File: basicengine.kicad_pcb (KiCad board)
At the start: 2 copper layers, 85 x 56 mm, 114 parts, among them J1 MicroSD Card, J10 Conn_01x01, J12 Conn_02x20_Counter_Clockwise, J17 PSX CONTROLLER, J2 USB KBD Alt, J3 Conn_01x06, J4 Conn_01x03, J5 VIDEO, J6 USB KBD, J7 AUDIO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

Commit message: pcb: add OSHW logo
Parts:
- added REF***: OSHW-Logo2_7.3x6mm_SilkScreen, Symbols:OSHW-Logo2_7.3x6mm_SilkScreen, B.Cu at (105.7, 118.3)

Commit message: pcb: follow sch oscillator capacitor change from 10p to 56p
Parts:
- C3, C4: value 10p -> 56p
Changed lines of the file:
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@@
       (effects (font (size 0.8128 0.8128) (thickness 0.15)) (justify mirror))
     )
-    (fp_text value 10p (at 1.63 -1.75 360) (layer B.SilkS)
+    (fp_text value 56p (at 1.63 -1.75 360) (layer B.SilkS)
       (effects (font (size 0.8128 0.8128) (thickness 0.15)) (justify mirror))
     )
@@
       (effects (font (size 0.8128 0.8128) (thickness 0.15)) (justify mirror))
     )
-    (fp_text value 10p (at -1.64 -1.65 180) (layer B.SilkS)
+    (fp_text value 56p (at -1.64 -1.65 180) (layer B.SilkS)
       (effects (font (size 0.8128 0.8128) (thickness 0.15)) (justify mirror))
     )

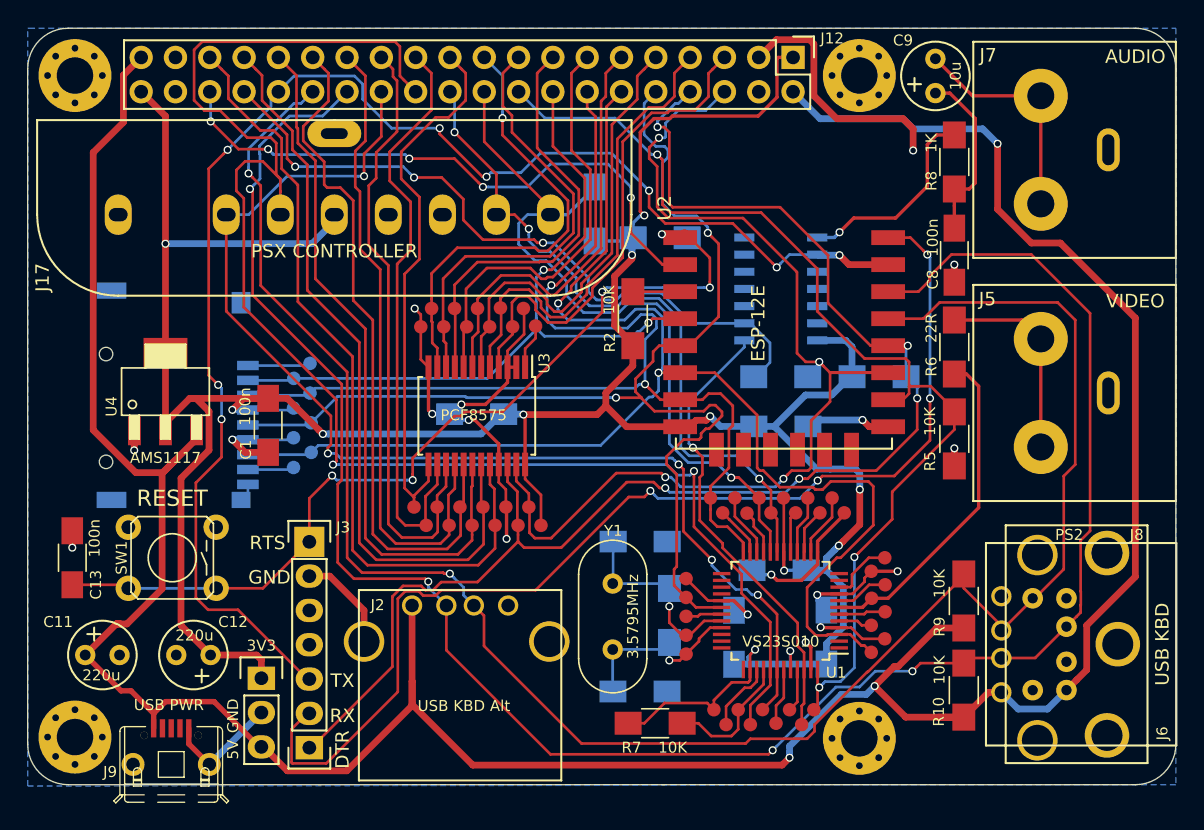
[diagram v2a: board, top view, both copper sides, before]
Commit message: pcb: revision 2
- follow sch in replacing electrolytics with ceramic SMT caps
- move J6 (primary USB KBD connector) left to reduce the proximity of
its pads to the shielding of J8 (PS/2 connector)
- move R9, R10 left to make space for J6
- move BASIC Engine logo down a bit
- update date and revision silkscreen
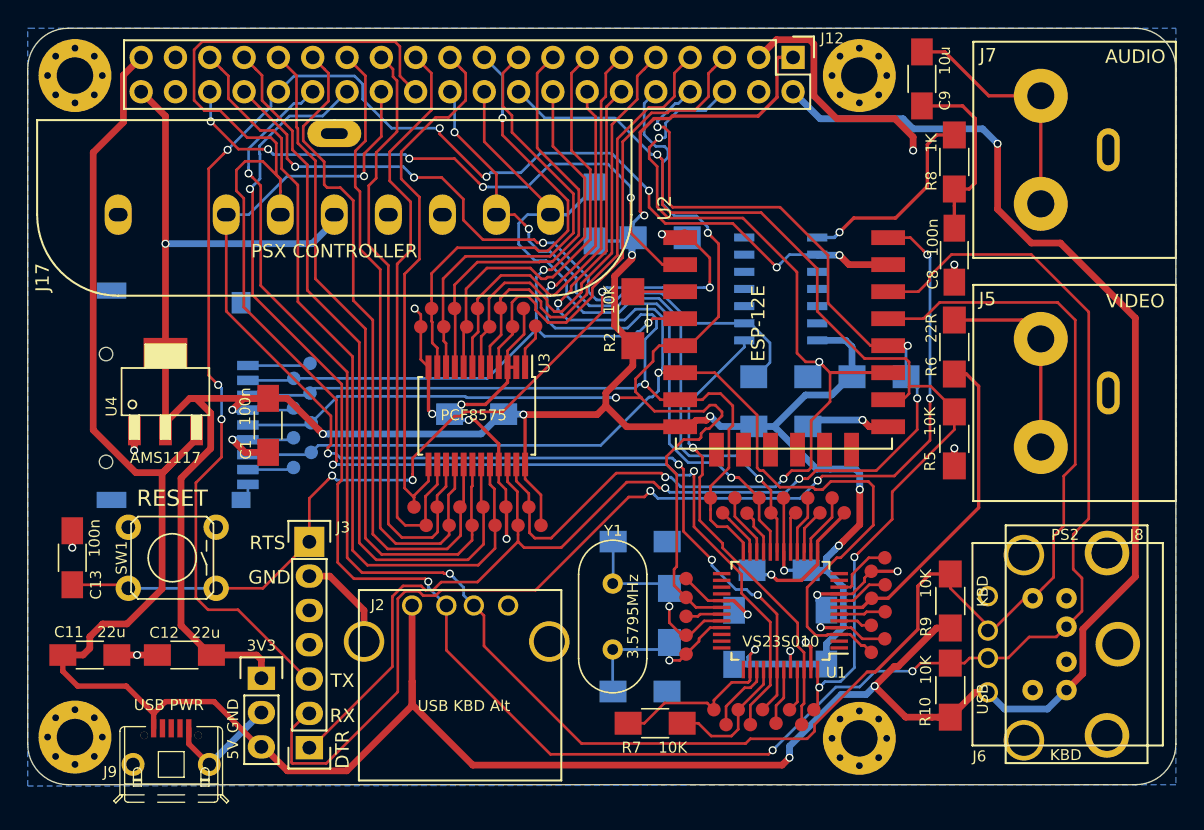
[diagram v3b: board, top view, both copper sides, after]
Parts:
- C11, C12: value 220u -> 22u; footprint Capacitors_Elko_ThroughHole:Elko_vert_11x5mm_RM2.5_CopperClear -> Capacitors_SMD:C_1206_HandSoldering
- C9: footprint Capacitors_Elko_ThroughHole:Elko_vert_11x5mm_RM2.5_CopperClear -> Capacitors_SMD:C_1206_HandSoldering
- J6: value USB KBD -> USB KBD
- moved C12 1.94 mm to (106.6, 116.4)
- moved C9 1.45 mm to (161.2, 73.8)
- moved J6 1.00 mm to (166.1, 119.2)
- moved R10 1.00 mm to (163.3, 119.0)
- moved R9 1.00 mm to (163.3, 112.4)
- moved G*** 0.50 mm to (135.5, 93.1)
- moved C11 0.34 mm to (99.6, 116.4)
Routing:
- net GND: track 122.1 -> 124.7 mm, vias 18 -> 19
- net /PS2_CLK: track 144.6 -> 146.5 mm
- net /5V: track 229.9 -> 231.5 mm
- net Net-(C9-Pad2): track 16.9 -> 18.1 mm
- net /PS2_DAT: track 150.9 -> 151.9 mm
- net Net-(C8-Pad1): track 13.1 -> 13.7 mm
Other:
- board text added: "BASIC Engine rev2"
- board text added: "KBD"
- board text added: "Uli 05/2018"
- board text removed: "BASIC Engine rev1"
- board text removed: "Uli 12/2017"
